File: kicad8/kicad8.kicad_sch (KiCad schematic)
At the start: 21 parts, among them J1 USB_C_Receptacle_USB2.0, U1 STM32F072CBT6, U2 PRTR5V0U2X

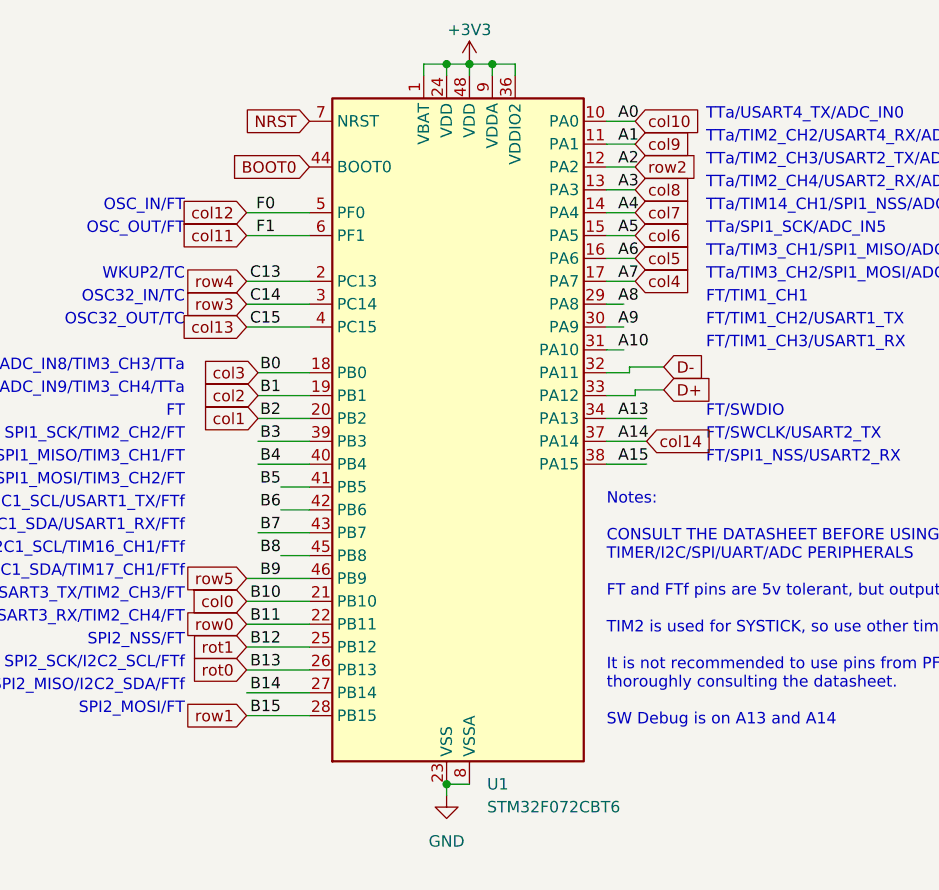
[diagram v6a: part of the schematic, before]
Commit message: Finished: Wiring for the Switch matrix, Underglow RGB and Per-key RGb
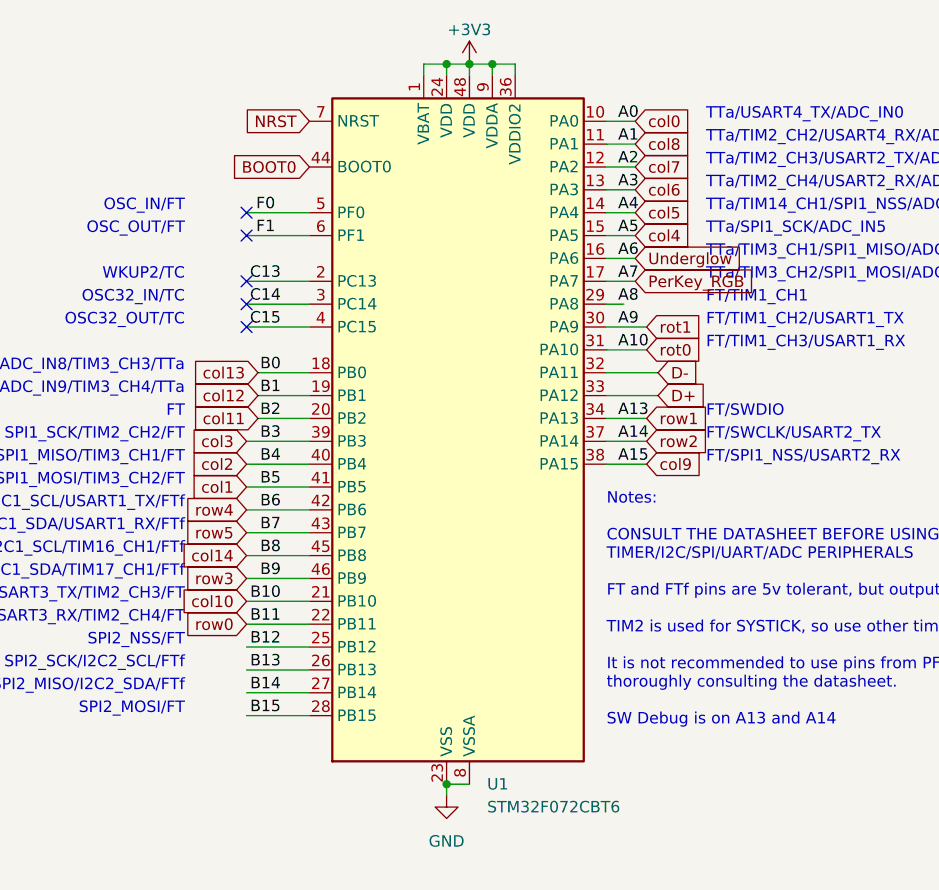
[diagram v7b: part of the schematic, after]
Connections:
- net A10 is gone; now on net rot0: U1.31 (PA10)
- net A13 is gone; now on net row1: U1.34 (PA13)
- net A15 is gone; now on net col9: U1.38 (PA15)
- net A9 is gone; now on net rot1: U1.30 (PA9)
- net B3 is gone; now on net col3: U1.39 (PB3)
- net B4 is gone; now on net col2: U1.40 (PB4)
- net B5 is gone; now on net col1: U1.41 (PB5)
- net B6 is gone; now on net row4: U1.42 (PB6)
- net B7 is gone; now on net row5: U1.43 (PB7)
- net B8 is gone; now on net col14: U1.45 (PB8)
- net col0: now also U1.10 (PA0); no longer U1.21 (PB10)
- net col1: no longer U1.20 (PB2)
- net col10: now also U1.21 (PB10); no longer U1.10 (PA0)
- net col11: now also U1.20 (PB2); no longer U1.6 (PF1)
- net col12: now also U1.19 (PB1); no longer U1.5 (PF0)
- net col13: now also U1.18 (PB0); no longer U1.4 (PC15)
- net col14: no longer U1.37 (PA14)
- net col2: no longer U1.19 (PB1)
- net col3: no longer U1.18 (PB0)
- net col4: now also U1.15 (PA5); no longer U1.17 (PA7)
- net col5: now also U1.14 (PA4); no longer U1.16 (PA6)
- net col6: now also U1.13 (PA3); no longer U1.15 (PA5)
- net col7: now also U1.12 (PA2); no longer U1.14 (PA4)
- net col8: now also U1.11 (PA1); no longer U1.13 (PA3)
- net col9: no longer U1.11 (PA1)
- net rot0: no longer U1.26 (PB13)
- net rot1: no longer U1.25 (PB12)
- net row1: no longer U1.28 (PB15)
- net row2: now also U1.37 (PA14); no longer U1.12 (PA2)
- net row3: now also U1.46 (PB9); no longer U1.3 (PC14)
- net row4: no longer U1.2 (PC13)
- net row5: no longer U1.46 (PB9)
- new net B12: U1.25 (PB12)
- new net B13: U1.26 (PB13)
- new net B15: U1.28 (PB15)
- new net C13: U1.2 (PC13)
- new net C14: U1.3 (PC14)
- new net C15: U1.4 (PC15)
- new net F0: U1.5 (PF0)
- new net F1: U1.6 (PF1)
- new net PerKey_RGB: U1.17 (PA7)
- new net Underglow: U1.16 (PA6)
- no-connect marks 2 -> 7

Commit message: Initial branch commit
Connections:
- net A8 is gone; now on net col2: U1.29 (PA8)
- net B12 is gone; now on net col6: U1.25 (PB12)
- net B13 is gone; now on net col5: U1.26 (PB13)
- net B14 is gone; now on net col4: U1.27 (PB14)
- net B15 is gone; now on net col3: U1.28 (PB15)
- net PerKey_RGB: now also U1.41 (PB5); no longer U1.17 (PA7)
- net Underglow: now also U1.19 (PB1); no longer U1.16 (PA6)
- net col0: now also U1.31 (PA10); no longer U1.10 (PA0)
- net col1: now also U1.30 (PA9); no longer U1.41 (PB5)
- net col10: now also U1.15 (PA5); no longer U1.21 (PB10)
- net col11: now also U1.14 (PA4); no longer U1.20 (PB2)
- net col12: now also U1.13 (PA3); no longer U1.19 (PB1)
- net col13: now also U1.43 (PB7); no longer U1.18 (PB0)
- net col14: now also U1.42 (PB6); no longer U1.45 (PB8)
- net col2: no longer U1.40 (PB4)
- net col3: no longer U1.39 (PB3)
- net col4: no longer U1.15 (PA5)
- net col5: no longer U1.14 (PA4)
- net col6: no longer U1.13 (PA3)
- net col7: now also U1.22 (PB11); no longer U1.12 (PA2)
- net col8: now also U1.21 (PB10); no longer U1.11 (PA1)
- net col9: now also U1.16 (PA6); no longer U1.38 (PA15)
- net rot0: now also U1.45 (PB8); no longer U1.31 (PA10)
- net rot1: now also U1.46 (PB9); no longer U1.30 (PA9)
- net row0: now also U1.34 (PA13); no longer U1.22 (PB11)
- net row1: now also U1.20 (PB2); no longer U1.34 (PA13)
- net row2: now also U1.17 (PA7); no longer U1.37 (PA14)
- net row3: now also U1.10 (PA0); no longer U1.46 (PB9)
- net row4: now also U1.12 (PA2); no longer U1.42 (PB6)
- net row5: now also U1.11 (PA1); no longer U1.43 (PB7)
- new net A14: U1.37 (PA14)
- new net A15: U1.38 (PA15)
- new net B0: U1.18 (PB0)
- new net B3: U1.39 (PB3)
- new net B4: U1.40 (PB4)
